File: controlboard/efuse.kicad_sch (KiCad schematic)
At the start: 13 parts, among them U2 TPS25963x

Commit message: schematic improvements
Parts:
- added SW1: SW_Push TODO FP CHECK, Button_Switch_SMD:SW_SPST_SKQG_WithStem, symbol Switch:SW_Push
- added TP8: TestPoint, symbol Connector:TestPoint
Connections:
- net GND: now also SW1.1
- net OUT: now also TP8.1
- net at R42.2, R43.1, U2.3 (EN/UVLO): now also SW1.2
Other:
- note added: "Reset Switch"
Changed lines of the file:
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@@
+	)
+	(junction
+		(at 146.05 82.55)
+		(diameter 0)
+		(color 0 0 0 0)
 	)
 	(junction
@@
 	)
 	(junction
+		(at 95.25 93.98)
+		(diameter 0)
+		(color 0 0 0 0)
+	)
+	(junction
 		(at 142.24 82.55)
 		(diameter 0)
@@
 	(wire
 		(pts
+			(xy 80.01 93.98) (xy 95.25 93.98)
+		)
+		(stroke
+			(width 0)
+			(type default)
+		)
+	)
+	(wire
+		(pts
+			(xy 146.05 82.55) (xy 142.24 82.55)
+		)
+		(stroke
+			(width 0)
+			(type default)
+		)
+	)
+	(wire
+		(pts
 			(xy 95.25 60.96) (xy 121.92 60.96)
 		)
@@
 	(wire
 		(pts
+			(xy 80.01 74.93) (xy 95.25 74.93)
+		)
+		(stroke
+			(width 0)
+			(type default)
+		)
+	)
+	(wire
+		(pts
 			(xy 142.24 91.44) (xy 142.24 90.17)
 		)
@@
 	(wire
 		(pts
+			(xy 80.01 90.17) (xy 80.01 93.98)
+		)
+		(stroke
+			(width 0)
+			(type default)
+		)
+	)
+	(wire
+		(pts
 			(xy 163.83 41.91) (xy 163.83 44.45)
 		)
@@
 	(wire
 		(pts
-			(xy 148.59 82.55) (xy 142.24 82.55)
+			(xy 148.59 82.55) (xy 146.05 82.55)
 		)
 		(stroke
@@
 			(width 0)
 			(type default)
+		)
+	)
+	(wire
+		(pts
+			(xy 80.01 80.01) (xy 80.01 74.93)
+		)
+		(stroke
+			(width 0)
+			(type default)
+		)
+	)
+	(text "Reset Switch"
+		(exclude_from_sim no)
+		(at 72.136 81.28 0)
+		(effects
+			(font
+				(size 1.27 1.27)
+			)
 		)
 	)
@@
 	)
 	(symbol
+		(lib_id "Switch:SW_Push")
+		(at 80.01 85.09 90)
+		(unit 1)
+		(exclude_from_sim no)
+		(in_bom yes)
+		(on_board yes)
+		(dnp no)
+		(property "Reference" "SW1"
+			(at 74.168 83.82 90)
+			(effects
+				(font
+					(size 1.27 1.27)
+				)
+				(justify right)
+			)
+		)
+		(property "Value" "SW_Push TODO FP CHECK"
+			(at 81.28 86.3599 90)
+			(effects
+				(font
+					(size 1.27 1.27)
+				)
+				(justify right)
+				(hide yes)
+			)
+		)
+		(property "Footprint" "Button_Switch_SMD:SW_SPST_SKQG_WithStem"
+			(at 74.93 85.09 0)
+			(effects
+				(font
+					(size 1.27 1.27)
+				)
+				(hide yes)
+			)
+		)
+		(property "Datasheet" "~"
+			(at 74.93 85.09 0)
+			(effects
+				(font
+					(size 1.27 1.27)
+				)
+				(hide yes)
+			)
+		)
+		(property "Description" "Push button switch, generic, two pins"
+			(at 80.01 85.09 0)
+			(effects
+				(font
+					(size 1.27 1.27)
+				)
+				(hide yes)
+			)
+		)
+		(pin "2"
+		)
+		(pin "1"
+		)
+		(instances
+			(project "controlboard"
+				(path "/2797250d-6fee-4769-b4dd-0e20ce4f0941/5fab4b81-761e-4fae-b113-00364a75fd9a/6730c4ed-849e-4137-aae0-c93a08939ea9"
+					(reference "SW1")
+					(unit 1)
+				)
+				(path "/2797250d-6fee-4769-b4dd-0e20ce4f0941/5fab4b81-761e-4fae-b113-00364a75fd9a/6f35b5a2-4903-498d-a87f-00926de2e745"
+					(reference "SW4")
+					(unit 1)
+				)
+				(path "/2797250d-6fee-4769-b4dd-0e20ce4f0941/5fab4b81-761e-4fae-b113-00364a75fd9a/c4ae39fe-dfab-4842-91d5-7d80cdea31e1"
+					(reference "SW5")
+					(unit 1)
+				)
+			)
+		)
+	)
+	(symbol
 		(lib_id "Device:R")
 		(at 109.22 90.17 0)
@@
 					(unit 1)
 				)
+			)
+		)
+	)
+	(symbol
+		(lib_id "Connector:TestPoint")
+		(at 146.05 82.55 0)
+		(unit 1)
+		(exclude_from_sim no)
+		(in_bom yes)
+		(on_board yes)
+		(dnp no)
+		(fields_autoplaced yes)
+		(property "Reference" "TP8"
+			(at 148.59 77.9779 0)
+			(effects
+				(font
+					(size 1.27 1.27)
+				)
+				(justify left)
+			)
+		)
+		(property "Value" "TestPoint"
+			(at 148.59 80.5179 0)
+			(effects
+				(font
+					(size 1.27 1.27)
+				)
+				(justify left)
+				(hide yes)
+			)
+		)
+		(property "Footprint" ""
+			(at 151.13 82.55 0)
+			(effects
+				(font
+					(size 1.27 1.27)
+				)
+				(hide yes)
+			)
+		)
+		(property "Datasheet" "~"
+			(at 151.13 82.55 0)
+			(effects
+				(font
+					(size 1.27 1.27)
+				)
+				(hide yes)
+			)
+		)
+		(property "Description" "test point"
+			(at 146.05 82.55 0)
+			(effects
+				(font
+					(size 1.27 1.27)
+				)
+				(hide yes)
+			)
+		)
+		(pin "1"
+		)
+		(instances
+			(project "controlboard"
+				(path "/2797250d-6fee-4769-b4dd-0e20ce4f0941/5fab4b81-761e-4fae-b113-00364a75fd9a/6730c4ed-849e-4137-aae0-c93a08939ea9"
+					(reference "TP8")
+					(unit 1)
+				)
+				(path "/2797250d-6fee-4769-b4dd-0e20ce4f0941/5fab4b81-761e-4fae-b113-00364a75fd9a/6f35b5a2-4903-498d-a87f-00926de2e745"
+					(reference "TP9")
+					(unit 1)
+				)
+				(path "/2797250d-6fee-4769-b4dd-0e20ce4f0941/5fab4b81-761e-4fae-b113-00364a75fd9a/c4ae39fe-dfab-4842-91d5-7d80cdea31e1"
+					(reference "TP10")
+					(unit 1)
+				)

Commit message: improvements
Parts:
- TP8: footprint (none) -> Connector_PinSocket_2.54mm:PinSocket_1x01_P2.54mm_Vertical
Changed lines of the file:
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@@
 			)
 		)
-		(property "Footprint" ""
+		(property "Footprint" "Connector_PinSocket_2.54mm:PinSocket_1x01_P2.54mm_Vertical"
 			(at 151.13 82.55 0)
 			(effects

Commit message: erc should be good now
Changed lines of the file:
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@@
+	)
+	(junction
+		(at 116.84 60.96)
+		(diameter 0)
+		(color 0 0 0 0)
 	)
 	(junction
@@
 	(wire
 		(pts
+			(xy 116.84 60.96) (xy 121.92 60.96)
+		)
+		(stroke
+			(width 0)
+			(type default)
+		)
+	)
+	(wire
+		(pts
 			(xy 120.65 90.17) (xy 121.92 90.17)
 		)
@@
 	(wire
 		(pts
-			(xy 95.25 60.96) (xy 121.92 60.96)
+			(xy 95.25 60.96) (xy 116.84 60.96)
 		)
 		(stroke
@@
 	)
 	(symbol
+		(lib_id "power:PWR_FLAG")
+		(at 116.84 60.96 0)
+		(unit 1)
+		(exclude_from_sim no)
+		(in_bom yes)
+		(on_board yes)
+		(dnp no)
+		(fields_autoplaced yes)
+		(property "Reference" "#FLG02"
+			(at 116.84 59.055 0)
+			(effects
+				(font
+					(size 1.27 1.27)
+				)
+				(hide yes)
+			)
+		)
+		(property "Value" "PWR_FLAG"
+			(at 116.84 55.88 0)
+			(effects
+				(font
+					(size 1.27 1.27)
+				)
+			)
+		)
+		(property "Footprint" ""
+			(at 116.84 60.96 0)
+			(effects
+				(font
+					(size 1.27 1.27)
+				)
+				(hide yes)
+			)
+		)
+		(property "Datasheet" "~"
+			(at 116.84 60.96 0)
+			(effects
+				(font
+					(size 1.27 1.27)
+				)
+				(hide yes)
+			)
+		)
+		(property "Description" "Special symbol for telling ERC where power comes from"
+			(at 116.84 60.96 0)
+			(effects
+				(font
+					(size 1.27 1.27)
+				)
+				(hide yes)
+			)
+		)
+		(pin "1"
+		)
+		(instances
+			(project "controlboard"
+				(path "/2797250d-6fee-4769-b4dd-0e20ce4f0941/5fab4b81-761e-4fae-b113-00364a75fd9a/6730c4ed-849e-4137-aae0-c93a08939ea9"
+					(reference "#FLG02")
+					(unit 1)
+				)
+				(path "/2797250d-6fee-4769-b4dd-0e20ce4f0941/5fab4b81-761e-4fae-b113-00364a75fd9a/6f35b5a2-4903-498d-a87f-00926de2e745"
+					(reference "#FLG03")
+					(unit 1)
+				)
+				(path "/2797250d-6fee-4769-b4dd-0e20ce4f0941/5fab4b81-761e-4fae-b113-00364a75fd9a/c4ae39fe-dfab-4842-91d5-7d80cdea31e1"
+					(reference "#FLG04")
+					(unit 1)
+				)
+			)
+		)
+	)
+	(symbol
 		(lib_id "Device:LED")
 		(at 137.16 64.77 270)
@@
 			)
 		)
-		(property "Description" ""
+		(property "Description" "Power symbol creates a global label with name \"GND\" , ground"
 			(at 171.45 52.07 0)
 			(effects
@@
 			)
 		)
-		(property "Description" ""
+		(property "Description" "Power symbol creates a global label with name \"GND\" , ground"
 			(at 120.65 93.98 0)
 			(effects
@@
 			)
 		)
-		(property "Description" ""
+		(property "Description" "Power symbol creates a global label with name \"GND\" , ground"
 			(at 163.83 52.07 0)
 			(effects

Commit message: pcb layout work
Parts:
- removed SW1: SW_Push TODO FP CHECK, Button_Switch_SMD:SW_SPST_SKQG_WithStem, symbol Switch:SW_Push
- added JP30: SolderJumper_2_Open, Jumper:SolderJumper-2_P1.3mm_Open_RoundedPad1.0x1.5mm, symbol Jumper:SolderJumper_2_Open
- TP8: footprint Connector_PinSocket_2.54mm:PinSocket_1x01_P2.54mm_Vertical -> TestPoint:TestPoint_THTPad_1.0x1.0mm_Drill0.5mm
- U2: footprint Package_SO:SOIC-8-1EP_3.9x4.9mm_P1.27mm_EP2.95x4.9mm_Mask2.71x3.4mm_ThermalVias -> Package_SO:TI_SO-PowerPAD-8
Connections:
- net GND: now also JP30.1 (A)
- net at R42.2, R43.1, U2.3 (EN/UVLO): now also JP30.2 (B)
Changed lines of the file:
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@@
 	(wire
 		(pts
-			(xy 80.01 90.17) (xy 80.01 93.98)
+			(xy 163.83 41.91) (xy 163.83 44.45)
 		)
 		(stroke
@@
 	(wire
 		(pts
-			(xy 163.83 41.91) (xy 163.83 44.45)
+			(xy 80.01 88.9) (xy 80.01 93.98)
 		)
 		(stroke
@@
 	(wire
 		(pts
-			(xy 80.01 80.01) (xy 80.01 74.93)
+			(xy 80.01 74.93) (xy 80.01 81.28)
 		)
 		(stroke
@@
 	)
 	(symbol
-		(lib_id "Switch:SW_Push")
-		(at 80.01 85.09 90)
-		(unit 1)
-		(exclude_from_sim no)
-		(in_bom yes)
-		(on_board yes)
-		(dnp no)
-		(property "Reference" "SW1"
-			(at 74.168 83.82 90)
-			(effects
-				(font
-					(size 1.27 1.27)
-				)
-				(justify right)
-			)
-		)
-		(property "Value" "SW_Push TODO FP CHECK"
-			(at 81.28 86.3599 90)
-			(effects
-				(font
-					(size 1.27 1.27)
-				)
-				(justify right)
-				(hide yes)
-			)
-		)
-		(property "Footprint" "Button_Switch_SMD:SW_SPST_SKQG_WithStem"
-			(at 74.93 85.09 0)
-			(effects
-				(font
-					(size 1.27 1.27)
-				)
-				(hide yes)
-			)
-		)
-		(property "Datasheet" "~"
-			(at 74.93 85.09 0)
-			(effects
-				(font
-					(size 1.27 1.27)
-				)
-				(hide yes)
-			)
-		)
-		(property "Description" "Push button switch, generic, two pins"
-			(at 80.01 85.09 0)
-			(effects
-				(font
-					(size 1.27 1.27)
-				)
-				(hide yes)
-			)
-		)
-		(pin "2"
-		)
-		(pin "1"
-		)
-		(instances
-			(project "controlboard"
-				(path "/2797250d-6fee-4769-b4dd-0e20ce4f0941/5fab4b81-761e-4fae-b113-00364a75fd9a/6730c4ed-849e-4137-aae0-c93a08939ea9"
-					(reference "SW1")
-					(unit 1)
-				)
-				(path "/2797250d-6fee-4769-b4dd-0e20ce4f0941/5fab4b81-761e-4fae-b113-00364a75fd9a/6f35b5a2-4903-498d-a87f-00926de2e745"
-					(reference "SW4")
-					(unit 1)
-				)
-				(path "/2797250d-6fee-4769-b4dd-0e20ce4f0941/5fab4b81-761e-4fae-b113-00364a75fd9a/c4ae39fe-dfab-4842-91d5-7d80cdea31e1"
-					(reference "SW5")
-					(unit 1)
-				)
-			)
-		)
-	)
-	(symbol
 		(lib_id "Device:R")
 		(at 109.22 90.17 0)
@@
 			)
 		)
-		(property "Footprint" "Connector_PinSocket_2.54mm:PinSocket_1x01_P2.54mm_Vertical"
+		(property "Footprint" "TestPoint:TestPoint_THTPad_1.0x1.0mm_Drill0.5mm"
 			(at 151.13 82.55 0)
 			(effects
@@
 			)
 		)
-		(property "Footprint" "Package_SO:SOIC-8-1EP_3.9x4.9mm_P1.27mm_EP2.95x4.9mm_Mask2.71x3.4mm_ThermalVias"
+		(property "Footprint" "Package_SO:TI_SO-PowerPAD-8"
 			(at 119.38 96.52 0)
 			(effects
@@
 					(unit 1)
 				)
+			)
+		)
+	)
+	(symbol
+		(lib_id "Jumper:SolderJumper_2_Open")
+		(at 80.01 85.09 270)
+		(mirror x)
+		(unit 1)
+		(exclude_from_sim yes)
+		(in_bom no)
+		(on_board yes)
+		(dnp no)
+		(property "Reference" "JP30"
+			(at 77.47 83.8199 90)
+			(effects
+				(font
+					(size 1.27 1.27)
+				)
+				(justify right)
+			)
+		)
+		(property "Value" "SolderJumper_2_Open"
+			(at 77.47 86.3599 90)
+			(effects
+				(font
+					(size 1.27 1.27)
+				)
+				(justify right)
+				(hide yes)
+			)
+		)
+		(property "Footprint" "Jumper:SolderJumper-2_P1.3mm_Open_RoundedPad1.0x1.5mm"
+			(at 80.01 85.09 0)
+			(effects
+				(font
+					(size 1.27 1.27)
+				)
+				(hide yes)
+			)
+		)
+		(property "Datasheet" "~"
+			(at 80.01 85.09 0)
+			(effects
+				(font
+					(size 1.27 1.27)
+				)
+				(hide yes)
+			)
+		)
+		(property "Description" "Solder Jumper, 2-pole, open"
+			(at 80.01 85.09 0)
+			(effects
+				(font
+					(size 1.27 1.27)
+				)
+				(hide yes)
+			)
+		)
+		(pin "2"
+		)
+		(pin "1"
+		)
+		(instances
+			(project "controlboard"
+				(path "/2797250d-6fee-4769-b4dd-0e20ce4f0941/5fab4b81-761e-4fae-b113-00364a75fd9a/c4ae39fe-dfab-4842-91d5-7d80cdea31e1"
+					(reference "JP30")
+					(unit 1)
+				)
+				(path "/2797250d-6fee-4769-b4dd-0e20ce4f0941/5fab4b81-761e-4fae-b113-00364a75fd9a/6730c4ed-849e-4137-aae0-c93a08939ea9"
+					(reference "JP19")
+					(unit 1)
+				)
+				(path "/2797250d-6fee-4769-b4dd-0e20ce4f0941/5fab4b81-761e-4fae-b113-00364a75fd9a/6f35b5a2-4903-498d-a87f-00926de2e745"
+					(reference "JP29")
+					(unit 1)
+				)

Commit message: improvements
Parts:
- R46: value 2k -> 3k
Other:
- note added: "1 to 7mA, reusing 3k value needed for ILim"
- note added: "RILIM: 903 / (lim - 0.0112) (11mA is rounding error tbh so: R = 903 / lim 3000ohm: .31A 1200ohm: .75A 470ohm: 1.92A Voltage limit calculator https://www.desmos.com/calculator/8uivoc5bgt 3.3V rail: (82k,20k,47k) 2.66V - 3.80V 5V rail: (150k,10k,47k) 4.34V - 5.29V Power rail: (150k, 47k, 12k) 4.25V - 20.9V Alt power rail: (150k, 47k, 15k) 4.10V - 17.0V (IC is only rated for 2.7V-19V so i don't want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"
- note removed: "RILIM: 903 / (lim - 0.0112) (11mA is rounding error tbh so: R = 903 / lim 3600ohm: .25A 1200ohm: .75A 470ohm: 1.92A Voltage limit calculator https://www.desmos.com/calculator/8uivoc5bgt 3.3V rail: (82k,20k,47k) 2.66V - 3.80V 5V rail: (150k,10k,47k) 4.34V - 5.29V Power rail: (150k, 47k, 12k) 4.25V - 20.9V Alt power rail: (150k, 47k, 15k) 4.10V - 17.0V (IC is only rated for 2.7V-19V so i don't want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"
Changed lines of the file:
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@@
+		)
+	)
+	(text "1 to 7mA, reusing 3k value needed for ILim"
+		(exclude_from_sim no)
+		(at 167.64 69.342 0)
+		(effects
+			(font
+				(size 1.27 1.27)
+			)
 		)
 	)
@@
 		)
 	)
-	(text "RILIM: 903 / (lim - 0.0112) (11mA is rounding error tbh so: R = 903 / lim\n\n3600ohm: .25A\n1200ohm: .75A\n470ohm: 1.92A\n\nVoltage limit calculator\nhttps://www.desmos.com/calculator/8uivoc5bgt\n\n3.3V rail: (82k,20k,47k) 2.66V - 3.80V\n5V rail: (150k,10k,47k)  4.34V - 5.29V\nPower rail: (150k, 47k, 12k) 4.25V - 20.9V\nAlt power rail: (150k, 47k, 15k) 4.10V - 17.0V\n\n(IC is only rated for 2.7V-19V so i don't want to risk it,\n but also having 20V would be cool for batteries (4s max = 17V)\n and just more power in general)"
+	(text "RILIM: 903 / (lim - 0.0112) (11mA is rounding error tbh so: R = 903 / lim\n\n3000ohm: .31A\n1200ohm: .75A\n470ohm: 1.92A\n\nVoltage limit calculator\nhttps://www.desmos.com/calculator/8uivoc5bgt\n\n3.3V rail: (82k,20k,47k) 2.66V - 3.80V\n5V rail: (150k,10k,47k)  4.34V - 5.29V\nPower rail: (150k, 47k, 12k) 4.25V - 20.9V\nAlt power rail: (150k, 47k, 15k) 4.10V - 17.0V\n\n(IC is only rated for 2.7V-19V so i don't want to risk it,\n but also having 20V would be cool for batteries (4s max = 17V)\n and just more power in general)"
 		(exclude_from_sim no)
 		(at 17.526 39.37 0)
@@
 			)
 		)
-		(property "Value" "2k"
+		(property "Value" "3k"
 			(at 140.97 72.39 90)
 			(effects

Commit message: controlboard finalized and ordered!!!
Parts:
- U2: JLCPCB Rotation Offset (none) -> -90
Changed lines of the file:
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@@
+			)
+		)
+		(property "JLCPCB Rotation Offset" ""
+			(at 171.45 48.26 0)
+			(effects
+				(font
+					(size 1.27 1.27)
+				)
+				(hide yes)
 			)
 		)
@@
 			)
 		)
+		(property "JLCPCB Rotation Offset" ""
+			(at 95.25 86.36 0)
+			(effects
+				(font
+					(size 1.27 1.27)
+				)
+				(hide yes)
+			)
+		)
 		(pin "1"
 		)
@@
 			)
 		)
+		(property "JLCPCB Rotation Offset" ""
+			(at 142.24 95.25 0)
+			(effects
+				(font
+					(size 1.27 1.27)
+				)
+				(hide yes)
+			)
+		)
 		(pin "2"
 		)
@@
 			)
 		)
+		(property "JLCPCB Rotation Offset" ""
+			(at 137.16 64.77 0)
+			(effects
+				(font
+					(size 1.27 1.27)
+				)
+				(hide yes)
+			)
+		)
 		(pin "1"
 		)
@@
 			)
 		)
+		(property "JLCPCB Rotation Offset" ""
+			(at 142.24 86.36 0)
+			(effects
+				(font
+					(size 1.27 1.27)
+				)
+				(hide yes)
+			)
+		)
 		(pin "1"
 		)
@@
 			)
 		)
+		(property "JLCPCB Rotation Offset" ""
+			(at 95.25 78.74 0)
+			(effects
+				(font
+					(size 1.27 1.27)
+				)
+				(hide yes)
+			)
+		)
 		(pin "1"
 		)
@@
 			)
 		)
+		(property "JLCPCB Rotation Offset" ""
+			(at 121.92 57.15 0)
+			(effects
+				(font
+					(size 1.27 1.27)
+				)
+				(hide yes)
+			)
+		)
 		(pin "2"
 		)
@@
 			)
 		)
+		(property "JLCPCB Rotation Offset" ""
+			(at 109.22 90.17 0)
+			(effects
+				(font
+					(size 1.27 1.27)
+				)
+				(hide yes)
+			)
+		)
 		(pin "1"
 		)
@@
 			)
 		)
+		(property "JLCPCB Rotation Offset" ""
+			(at 146.05 82.55 0)
+			(effects
+				(font
+					(size 1.27 1.27)
+				)
+				(hide yes)
+			)
+		)
 		(pin "1"
 		)
@@
 			)
 		)
+		(property "JLCPCB Rotation Offset" ""
+			(at 95.25 71.12 0)
+			(effects
+				(font
+					(size 1.27 1.27)
+				)
+				(hide yes)
+			)
+		)
 		(pin "1"
 		)
@@
 			)
 		)
+		(property "JLCPCB Rotation Offset" ""
+			(at 137.16 72.39 0)
+			(effects
+				(font
+					(size 1.27 1.27)
+				)
+				(hide yes)
+			)
+		)
 		(pin "2"
 		)
@@
 			)
 		)
+		(property "JLCPCB Rotation Offset" ""
+			(at 163.83 48.26 0)
+			(effects
+				(font
+					(size 1.27 1.27)
+				)
+				(hide yes)
+			)
+		)
 		(pin "2"
 		)
@@
 			)
 		)
+		(property "JLCPCB Rotation Offset" ""
+			(at 102.87 54.61 0)
+			(effects
+				(font
+					(size 1.27 1.27)
+				)
+				(hide yes)
+			)
+		)
 		(pin "2"
 		)
@@
 		)
 		(property "Description" "eFuse Protection Switch"
+			(at 120.65 80.01 0)
+			(effects
+				(font
+					(size 1.27 1.27)
+				)
+				(hide yes)
+			)
+		)
+		(property "JLCPCB Rotation Offset" "-90"
 			(at 120.65 80.01 0)
 			(effects
@@
 			(at 80.01 85.09 0)
 			(effects
+				(font
+					(size 1.27 1.27)
+				)
+				(hide yes)
+			)
+		)
+		(property "JLCPCB Rotation Offset" ""
+			(at 80.01 85.09 0)
+			(effects

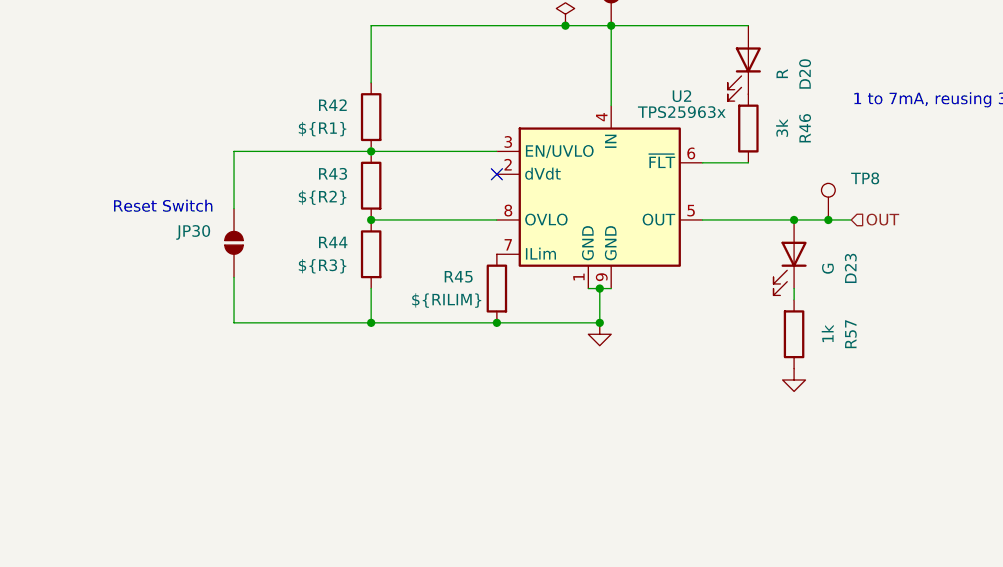
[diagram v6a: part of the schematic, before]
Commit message: Control board changes
Made a few control board changes (green checks on discord)
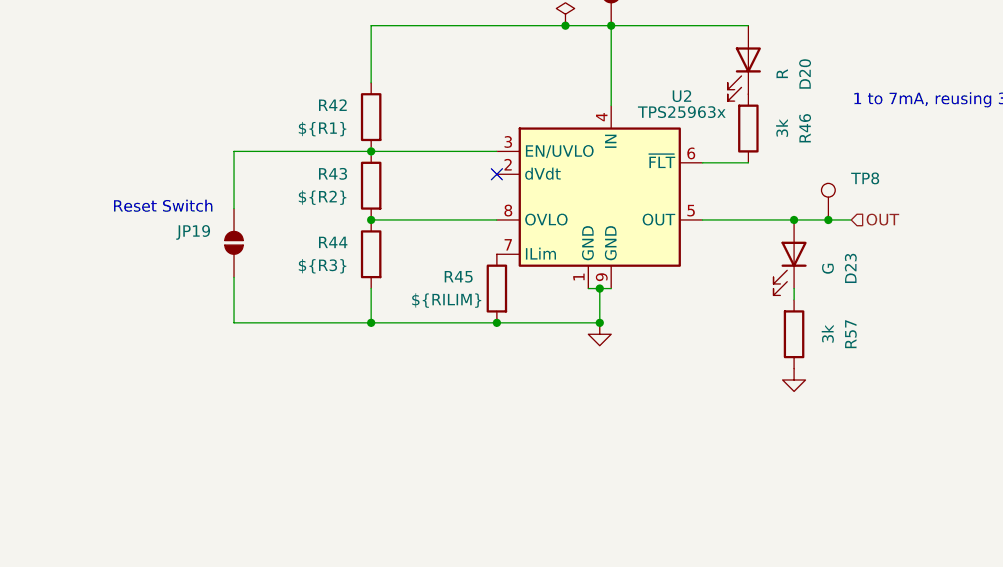
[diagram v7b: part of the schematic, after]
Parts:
- R57: value 1k -> 3k
- renumbered JP30 to JP19
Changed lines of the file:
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@@
 			)
 		)
-		(property "Value" "1k"
+		(property "Value" "3k"
 			(at 146.05 95.25 90)
 			(effects
@@
 		(on_board yes)
 		(dnp no)
-		(property "Reference" "JP30"
+		(property "Reference" "JP19"
 			(at 77.47 83.8199 90)
 			(effects
@@
 		(instances
 			(project "controlboard"
+				(path "/2797250d-6fee-4769-b4dd-0e20ce4f0941/5fab4b81-761e-4fae-b113-00364a75fd9a/6730c4ed-849e-4137-aae0-c93a08939ea9"
+					(reference "JP19")
+					(unit 1)
+				)
+				(path "/2797250d-6fee-4769-b4dd-0e20ce4f0941/5fab4b81-761e-4fae-b113-00364a75fd9a/6f35b5a2-4903-498d-a87f-00926de2e745"
+					(reference "JP29")
+					(unit 1)
+				)
 				(path "/2797250d-6fee-4769-b4dd-0e20ce4f0941/5fab4b81-761e-4fae-b113-00364a75fd9a/c4ae39fe-dfab-4842-91d5-7d80cdea31e1"
 					(reference "JP30")
 					(unit 1)
 				)
-				(path "/2797250d-6fee-4769-b4dd-0e20ce4f0941/5fab4b81-761e-4fae-b113-00364a75fd9a/6730c4ed-849e-4137-aae0-c93a08939ea9"
-					(reference "JP19")
-					(unit 1)
-				)
-				(path "/2797250d-6fee-4769-b4dd-0e20ce4f0941/5fab4b81-761e-4fae-b113-00364a75fd9a/6f35b5a2-4903-498d-a87f-00926de2e745"
-					(reference "JP29")
-					(unit 1)
-				)
